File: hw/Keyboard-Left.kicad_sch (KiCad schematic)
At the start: 18 parts, among them X3000 Mounting-Hole-M3, X3001 Mounting-Hole-M3, X3002 Mounting-Hole-M3, X3003 Mounting-Hole-M3, X3004 Distance-Bolt_M3x5, X3005 Distance-Bolt_M3x5, X3006 Distance-Bolt_M3x5, X3007 Distance-Bolt_M3x5, X3008 Screw M3x10, X3009 Screw M3x10, X3010 Screw M3x10, X3011 Screw M3x10, X3012 Screw M3x10, X3013 Screw M3x10, X3014 Screw M3x10, X3015 Screw M3x10

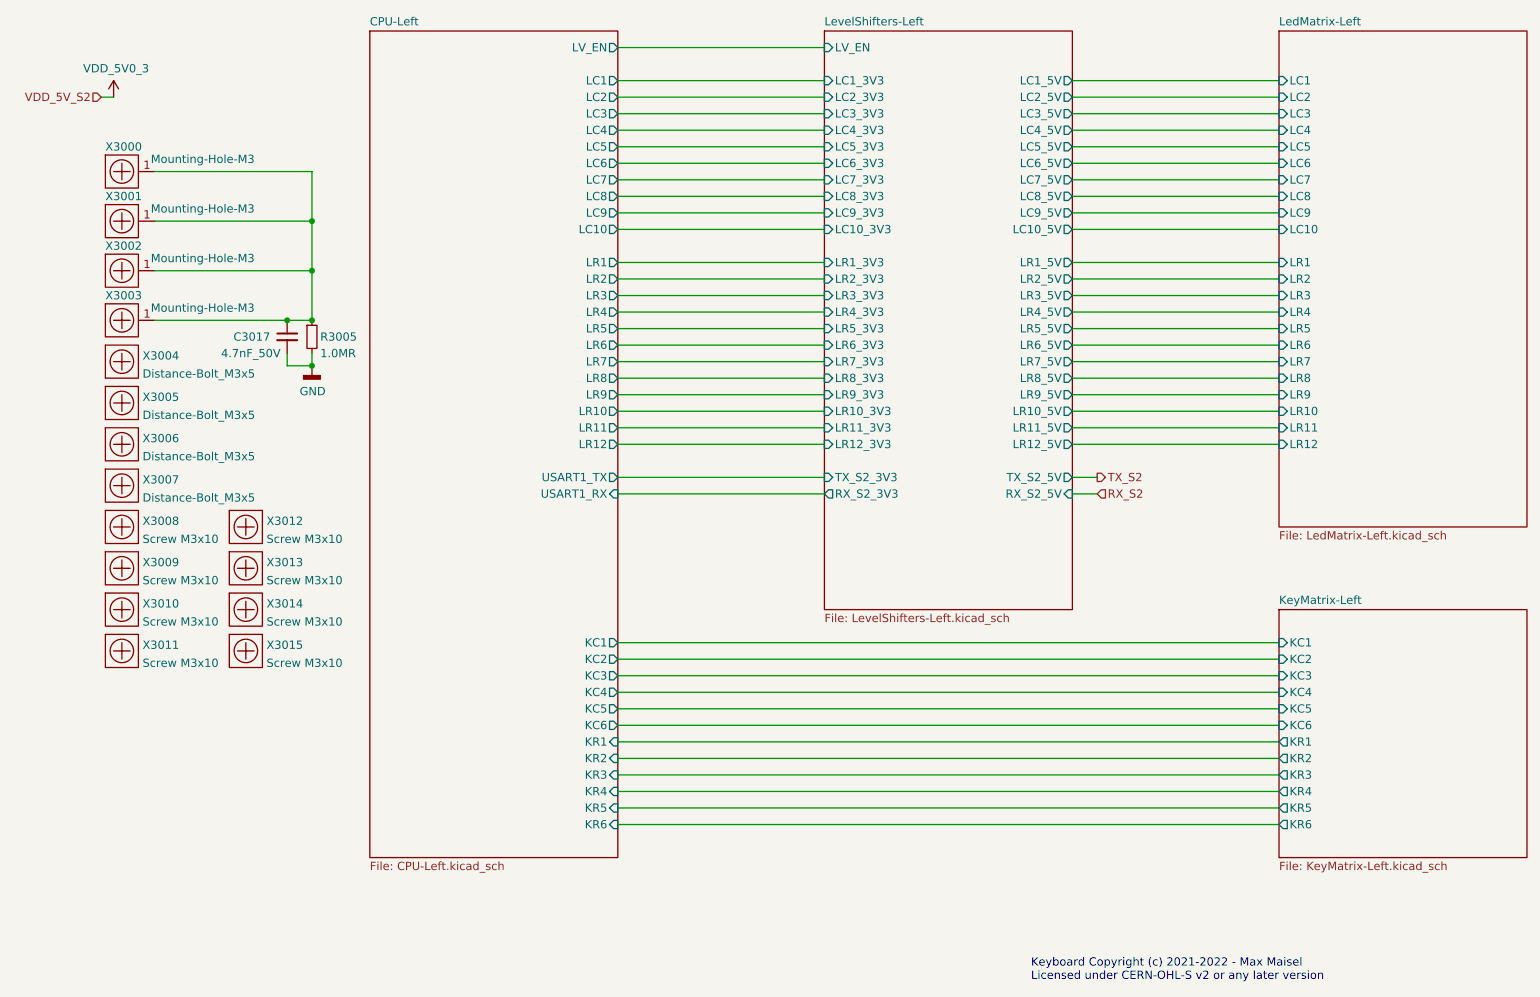
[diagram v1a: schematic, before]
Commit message: Update schematic:
- Add ESD protection.
- Adjust distance bolts so they fit to the MX mounting plate.
- Make key layout symmetric.
- Add resistor to TX driver outputs.
- Use alternate IO functions on inter-board connectors.
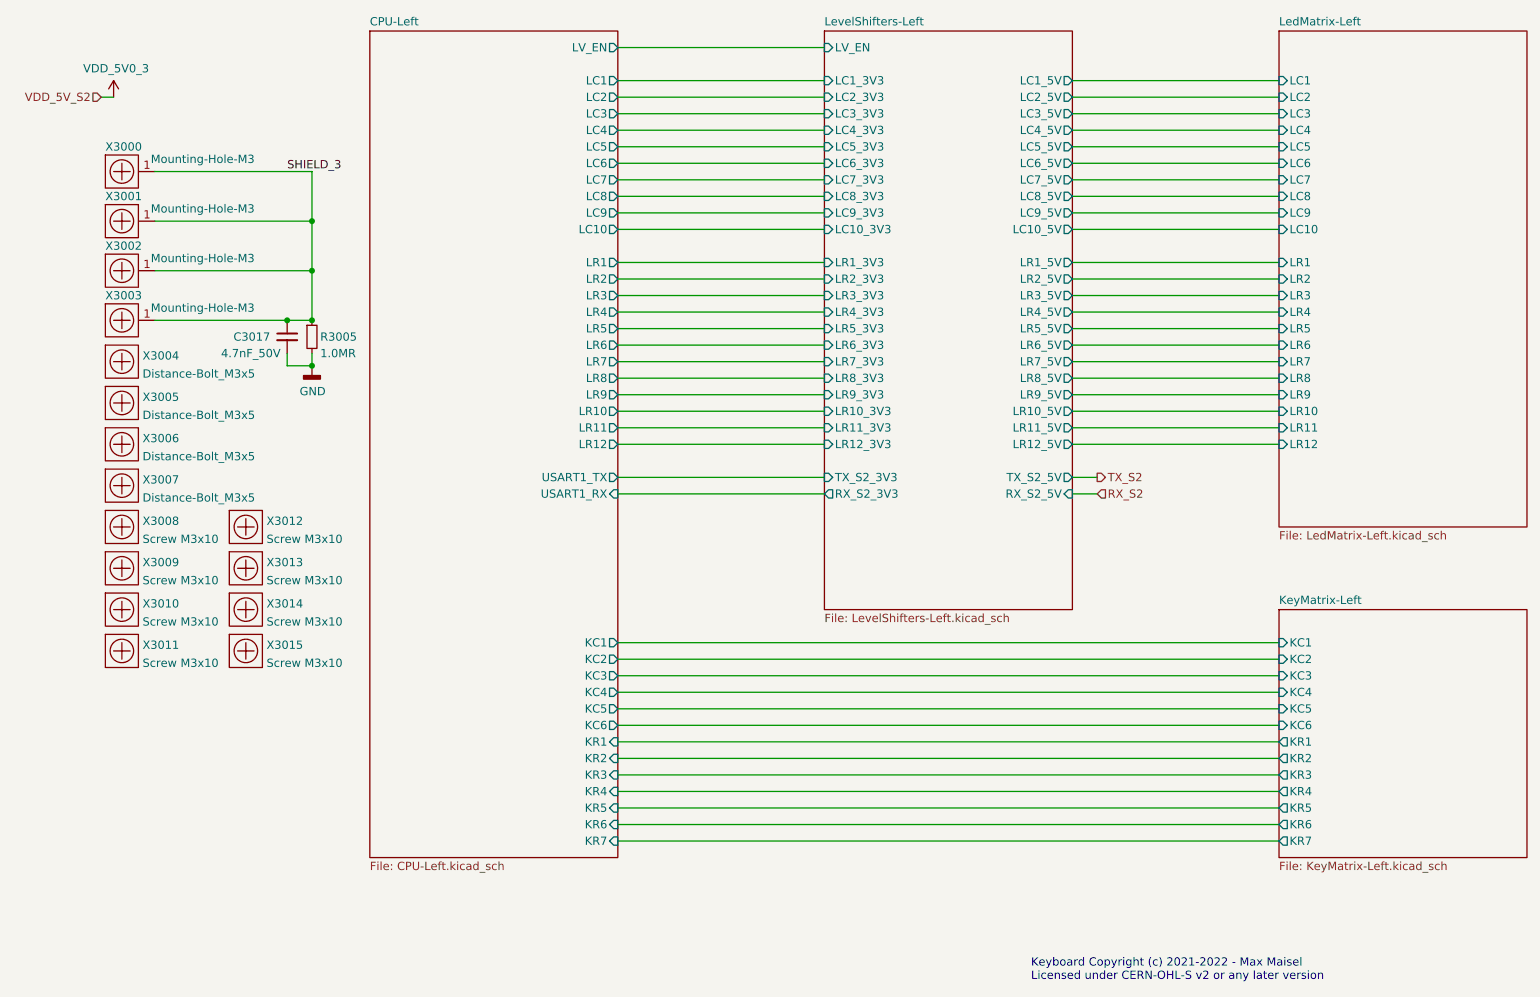
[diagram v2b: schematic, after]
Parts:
- X3004, X3005, X3006, X3007: footprint Keyboard:DistanceBolt-M3x5 -> Keyboard:DistanceBolt-6x3.5; symbol Keyboard:Distance-Bolt_M3x5 -> Keyboard:Distance-Bolt_6x3.5
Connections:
- net SHIELD_3: now reaches C3017.1, R3005.1, X3000.1, X3001.1, X3002.1, X3003.1
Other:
- sheet CPU-Left ports: added KR7; removed none
- sheet KeyMatrix-Left ports: added KR7; removed none
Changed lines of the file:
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@@
+    (stroke (width 0) (type default) (color 0 0 0 0))
+  )
+  (wire (pts (xy 215.9 149.86) (xy 114.3 149.86))
     (stroke (width 0) (type default) (color 0 0 0 0))
   )
@@
     (effects (font (size 1.27 1.27)) (justify left bottom))
   )
+  (label "SHIELD_3" (at 63.5 46.99 0)
+    (effects (font (size 1.27 1.27)) (justify left bottom))
+  )
   (hierarchical_label "VDD_5V_S2" (shape input) (at 34.925 35.56 180)
     (effects (font (size 1.27 1.27)) (justify right))
@@
     (pin "1")
   )
-  (symbol (lib_id "Keyboard:Distance-Bolt_M3x5") (at 38.1 82.55 0) (unit 1)
+  (symbol (lib_id "Keyboard:Distance-Bolt_6x3.5") (at 38.1 82.55 0) (unit 1)
     (in_bom yes) (on_board yes) (fields_autoplaced)
     (property "Reference" "X3005" (id 0) (at 41.275 81.6415 0)
@@
       (effects (font (size 1.27 1.27)) (justify left))
     )
-    (property "Footprint" "Keyboard:DistanceBolt-M3x5" (id 2) (at 38.1 82.55 0)
+    (property "Footprint" "Keyboard:DistanceBolt-6x3.5" (id 2) (at 38.1 82.55 0)
       (effects (font (size 1.27 1.27)) hide)
     )
@@
     )
   )
-  (symbol (lib_id "Keyboard:Distance-Bolt_M3x5") (at 38.1 76.2 0) (unit 1)
+  (symbol (lib_id "Keyboard:Distance-Bolt_6x3.5") (at 38.1 76.2 0) (unit 1)
     (in_bom yes) (on_board yes) (fields_autoplaced)
     (property "Reference" "X3004" (id 0) (at 41.275 75.2915 0)
@@
       (effects (font (size 1.27 1.27)) (justify left))
     )
-    (property "Footprint" "Keyboard:DistanceBolt-M3x5" (id 2) (at 38.1 76.2 0)
+    (property "Footprint" "Keyboard:DistanceBolt-6x3.5" (id 2) (at 38.1 76.2 0)
       (effects (font (size 1.27 1.27)) hide)
     )
@@
     )
   )
-  (symbol (lib_id "Keyboard:Distance-Bolt_M3x5") (at 38.1 95.25 0) (unit 1)
+  (symbol (lib_id "Keyboard:Distance-Bolt_6x3.5") (at 38.1 95.25 0) (unit 1)
     (in_bom yes) (on_board yes) (fields_autoplaced)
     (property "Reference" "X3007" (id 0) (at 41.275 94.3415 0)
@@
       (effects (font (size 1.27 1.27)) (justify left))
     )
-    (property "Footprint" "Keyboard:DistanceBolt-M3x5" (id 2) (at 38.1 95.25 0)
+    (property "Footprint" "Keyboard:DistanceBolt-6x3.5" (id 2) (at 38.1 95.25 0)
       (effects (font (size 1.27 1.27)) hide)
     )
@@
     )
   )
-  (symbol (lib_id "Keyboard:Distance-Bolt_M3x5") (at 38.1 88.9 0) (unit 1)
+  (symbol (lib_id "Keyboard:Distance-Bolt_6x3.5") (at 38.1 88.9 0) (unit 1)
     (in_bom yes) (on_board yes) (fields_autoplaced)
     (property "Reference" "X3006" (id 0) (at 41.275 87.9915 0)
@@
       (effects (font (size 1.27 1.27)) (justify left))
     )
-    (property "Footprint" "Keyboard:DistanceBolt-M3x5" (id 2) (at 38.1 88.9 0)
+    (property "Footprint" "Keyboard:DistanceBolt-6x3.5" (id 2) (at 38.1 88.9 0)
       (effects (font (size 1.27 1.27)) hide)
     )
@@
       (effects (font (size 1.27 1.27)) (justify left))
     )
+    (pin "KR7" output (at 215.9 149.86 180)
+      (effects (font (size 1.27 1.27)) (justify left))
+    )
   )
   (sheet (at 215.9 25.4) (size 38.1 76.2) (fields_autoplaced)
@@
       (effects (font (size 1.27 1.27)) (justify right))
     )
+    (pin "KR7" input (at 114.3 149.86 0)
+      (effects (font (size 1.27 1.27)) (justify right))
+    )
